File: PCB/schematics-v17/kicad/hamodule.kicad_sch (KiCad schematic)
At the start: 84 parts, among them J1 2604-1104, J10 EspSense, J11 Conn_01x02_Male, J12 DoNotCon->, J2 2604-1102, J3 USB_C_Receptacle_USB2.0, J4 ESP Relays, J5 Current Jumper, J6 GND 3.3V, J7 Conn_01x02, J8 Current Jumper, J9 2604-1104, K1 PCN-105D, K2 PCN-105D, K3 PCN-105D, K4 PCN-105D, Q1 SS8050-SMD, Q2 SS8050, SW1 EN, SW2 IO0, U1 ULN2003A, U2 ESP32-WROOM-32E, U4 LD1117AV33_TO220, U5 MCP9700T-ETT, U6 LDA210-PDIP, U7 LDA210-PDIP, U8 CP2102N-A01-GQFN28

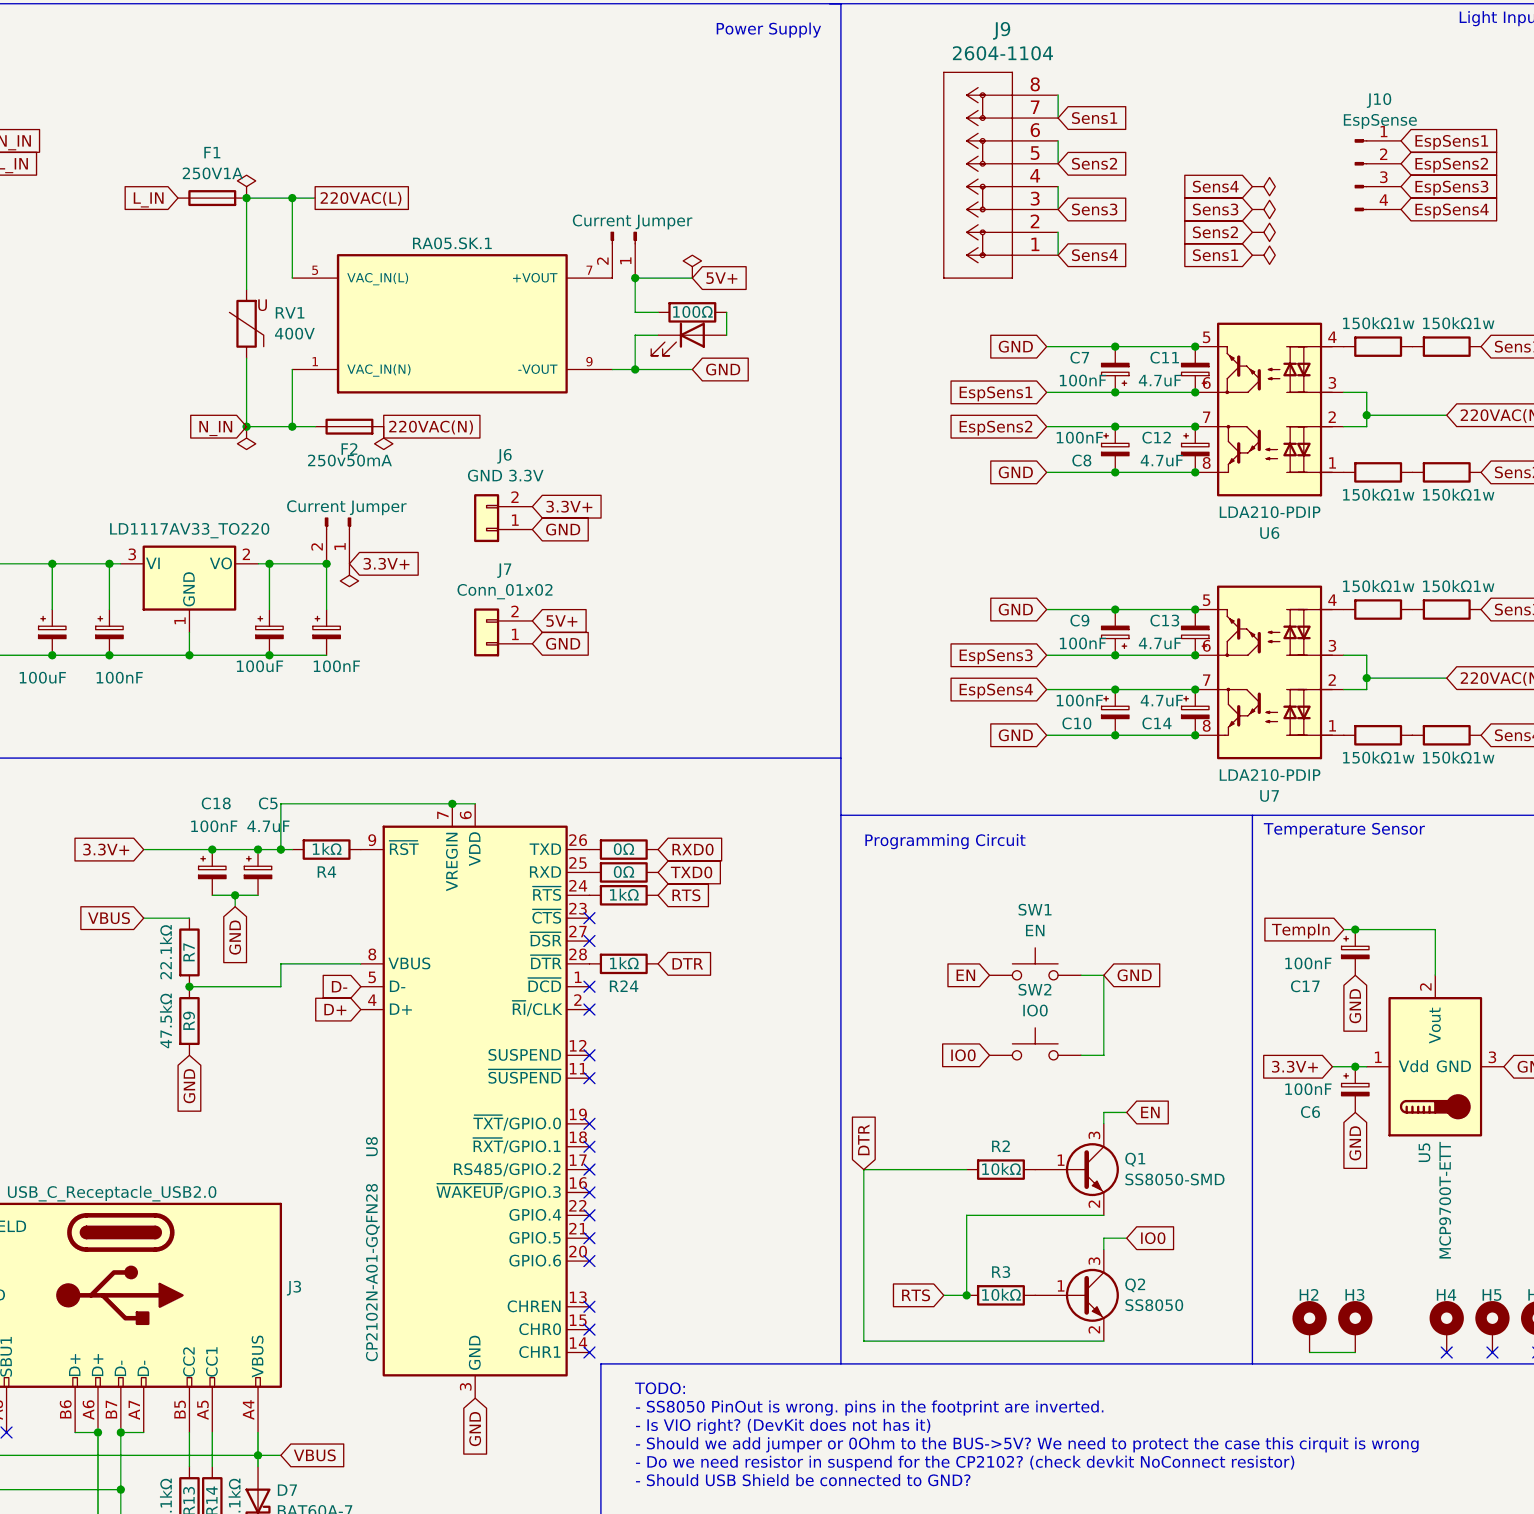
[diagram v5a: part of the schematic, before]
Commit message: GPIO34+ do not have pull-ups, adding them in hardware
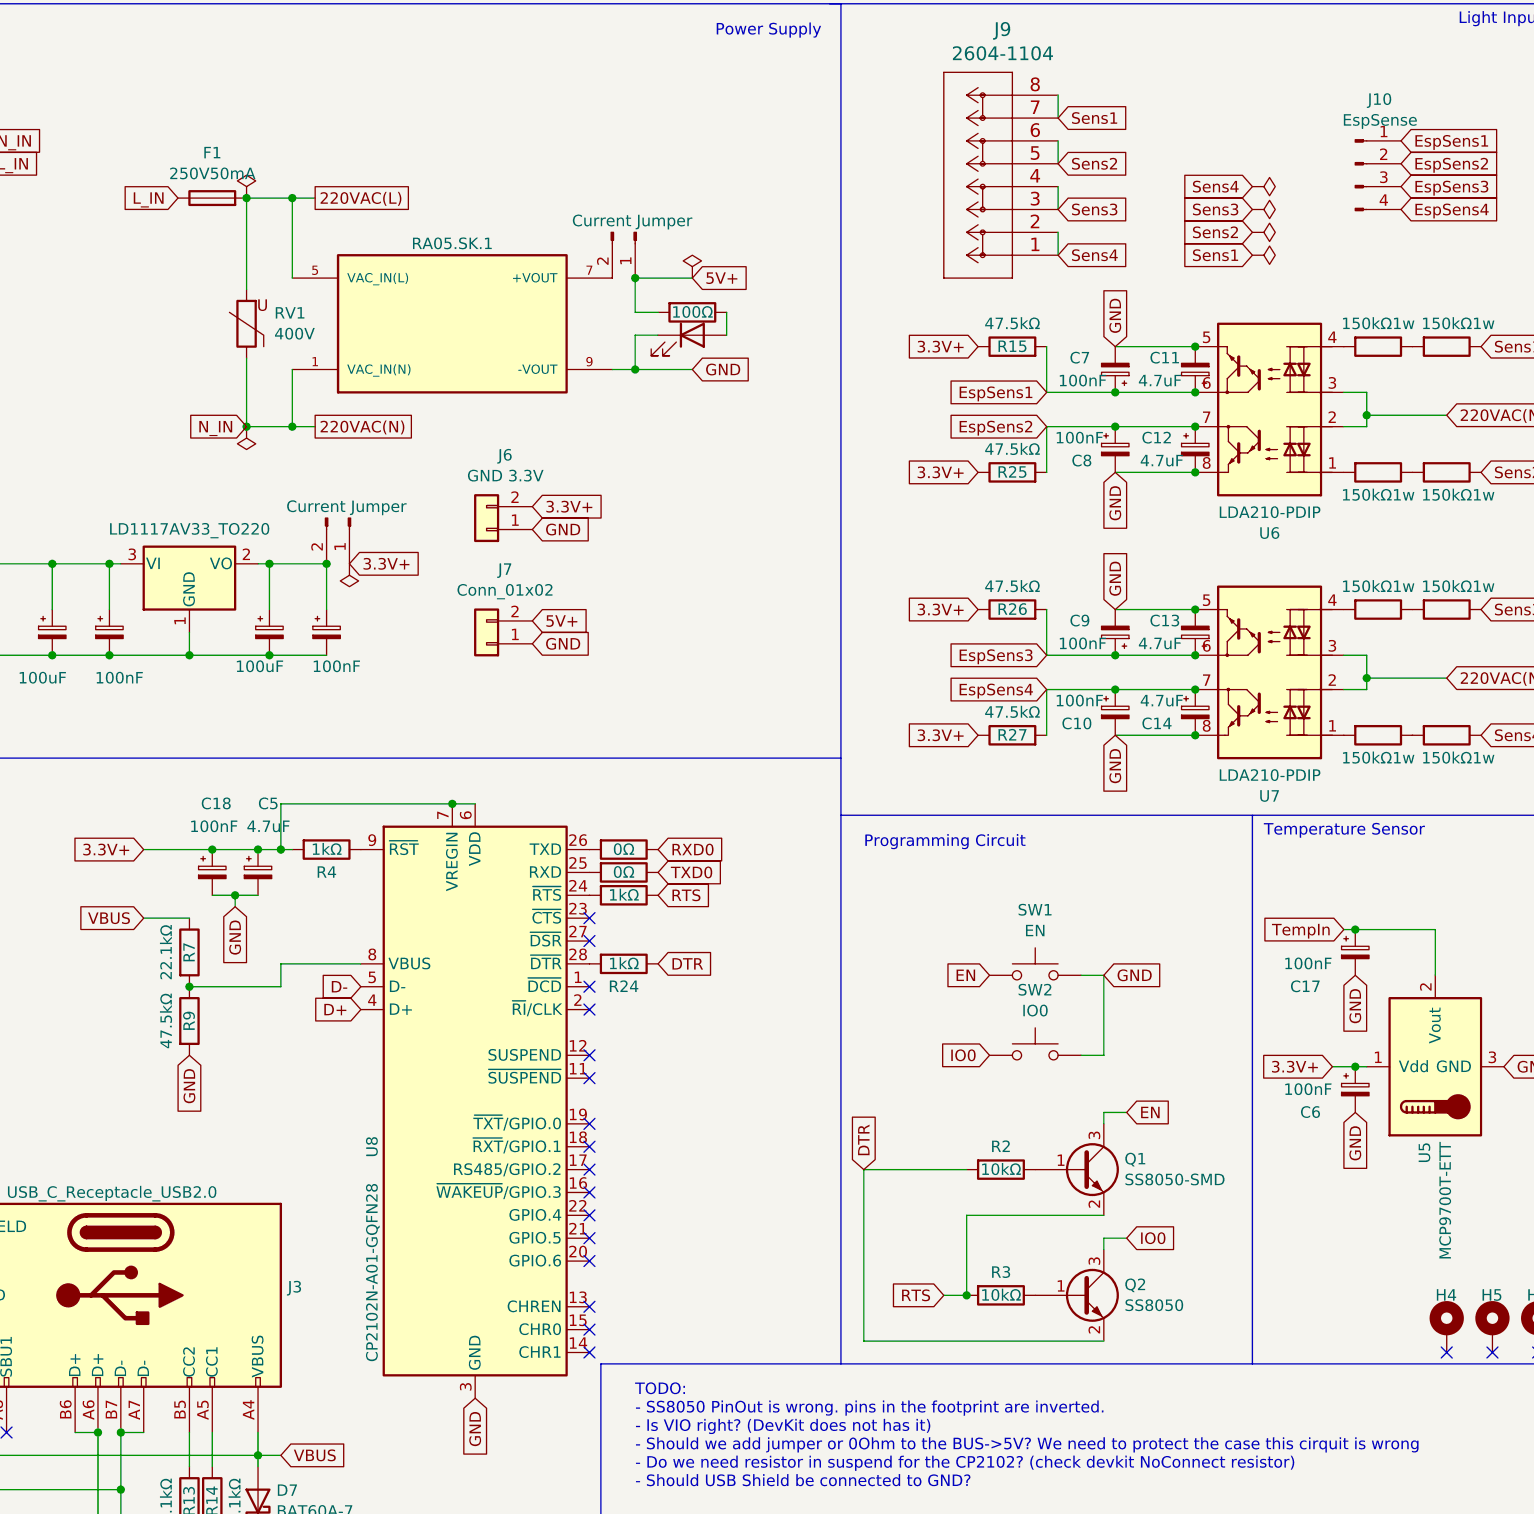
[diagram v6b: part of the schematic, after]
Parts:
- removed F2: 250v50mA, Fuse:Fuse_Littelfuse_372_D8.50mm, symbol Device:Fuse
- removed H2, H3: MountingHole_Pad, MountingHole:MountingHole_2.2mm_M2_DIN965_Pad_TopOnly, symbol Mechanical:MountingHole_Pad
- added R15, R25, R26, R27: 47.5kΩ, Resistor_SMD:R_0603_1608Metric_Pad0.98x0.95mm_HandSolder, symbol Device:R
- F1: value 250V1A -> 250V50mA
- renumbered 100uF_2 to C19, 100uF_1 to C?
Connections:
- net N_IN is gone; now on net 220VAC(N): J2.3, J2.4, RA05.SK.1.1 (VAC_IN(N)), RV1.1
- net 3.3V+: now also R15.1, R25.1, R26.1, R27.1
- net EspSens1: now also R15.2
- net EspSens2: now also R25.2
- net EspSens3: now also R26.2
- net EspSens4: now also R27.2

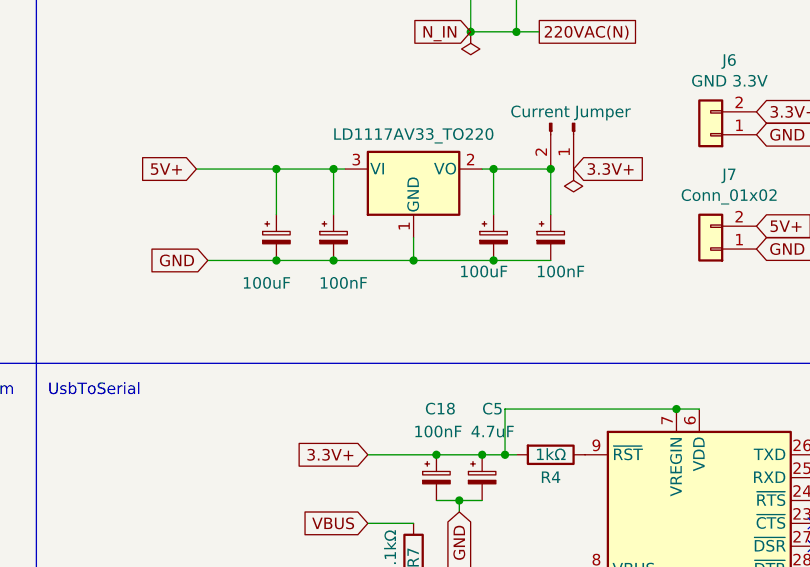
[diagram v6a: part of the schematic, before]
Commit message: fixing electrolytic Capacitor values
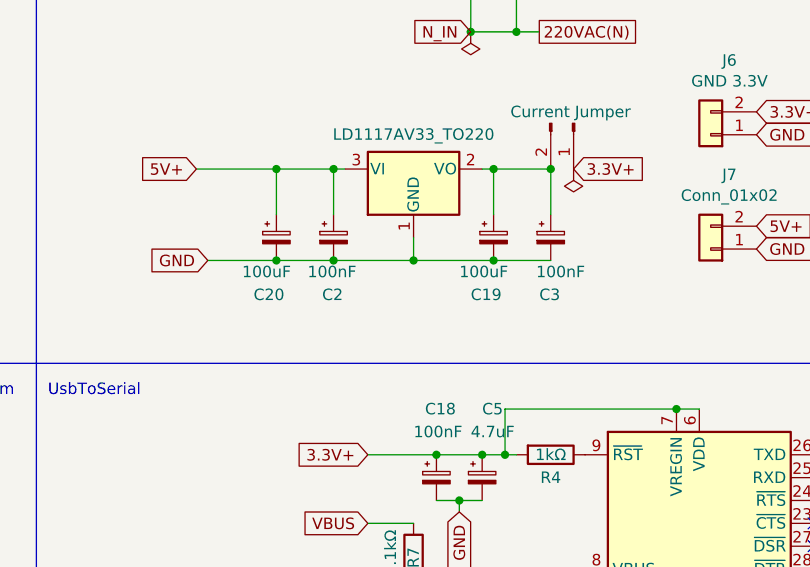
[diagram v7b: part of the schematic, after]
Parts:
- gave numbers to parts that had none: 1
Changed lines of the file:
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@@
   (symbol (lib_id "Device:C_Polarized_Small") (at 114.3 83.82 0) (unit 1)
     (in_bom yes) (on_board yes)
-    (property "Reference" "C?" (id 0) (at 117.2972 82.6516 0)
-      (effects (font (size 1.27 1.27)) (justify left) hide)
-    )
-    (property "Value" "100uF" (id 1) (at 110.49 88.9 0)
+    (property "Reference" "C20" (id 0) (at 111.76 90.17 0)
+      (effects (font (size 1.27 1.27)) (justify left))
+    )
+    (property "Value" "100uF" (id 1) (at 110.49 87.63 0)
       (effects (font (size 1.27 1.27)) (justify left))
     )
@@
   (symbol (lib_id "Device:C_Polarized_Small") (at 138.43 83.82 0) (unit 1)
     (in_bom yes) (on_board yes)
-    (property "Reference" "C19" (id 0) (at 141.4272 82.6516 0)
-      (effects (font (size 1.27 1.27)) (justify left) hide)
+    (property "Reference" "C19" (id 0) (at 135.89 90.17 0)
+      (effects (font (size 1.27 1.27)) (justify left))
     )
     (property "Value" "100uF" (id 1) (at 134.62 87.63 0)
@@
   (symbol (lib_id "Device:C_Polarized_Small") (at 120.65 83.82 0) (unit 1)
     (in_bom yes) (on_board yes)
-    (property "Reference" "C2" (id 0) (at 123.6472 82.6516 0)
-      (effects (font (size 1.27 1.27)) (justify left) hide)
-    )
-    (property "Value" "100nF" (id 1) (at 124.46 88.9 0)
+    (property "Reference" "C2" (id 0) (at 119.38 90.17 0)
+      (effects (font (size 1.27 1.27)) (justify left))
+    )
+    (property "Value" "100nF" (id 1) (at 123.19 87.63 0)
       (effects (font (size 1.27 1.27)) (justify right))
     )
@@
   (symbol (lib_id "Device:C_Polarized_Small") (at 144.78 83.82 0) (unit 1)
     (in_bom yes) (on_board yes)
-    (property "Reference" "C3" (id 0) (at 147.7772 82.6516 0)
-      (effects (font (size 1.27 1.27)) (justify left) hide)
+    (property "Reference" "C3" (id 0) (at 143.51 90.17 0)
+      (effects (font (size 1.27 1.27)) (justify left))
     )
     (property "Value" "100nF" (id 1) (at 148.59 87.63 0)
@@
     )
     (path "/00000000-0000-0000-0000-00006151dfd1"
-      (reference "C?") (unit 1) (value "100uF") (footprint "Capacitor_THT:CP_Radial_D6.3mm_P2.50mm")
+      (reference "C20") (unit 1) (value "100uF") (footprint "Capacitor_THT:CP_Radial_D6.3mm_P2.50mm")
     )
     (path "/00000000-0000-0000-0000-0000619d076d"
